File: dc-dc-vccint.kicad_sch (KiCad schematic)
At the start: 61 parts, among them U36 MP8796B, U4 MP8796B

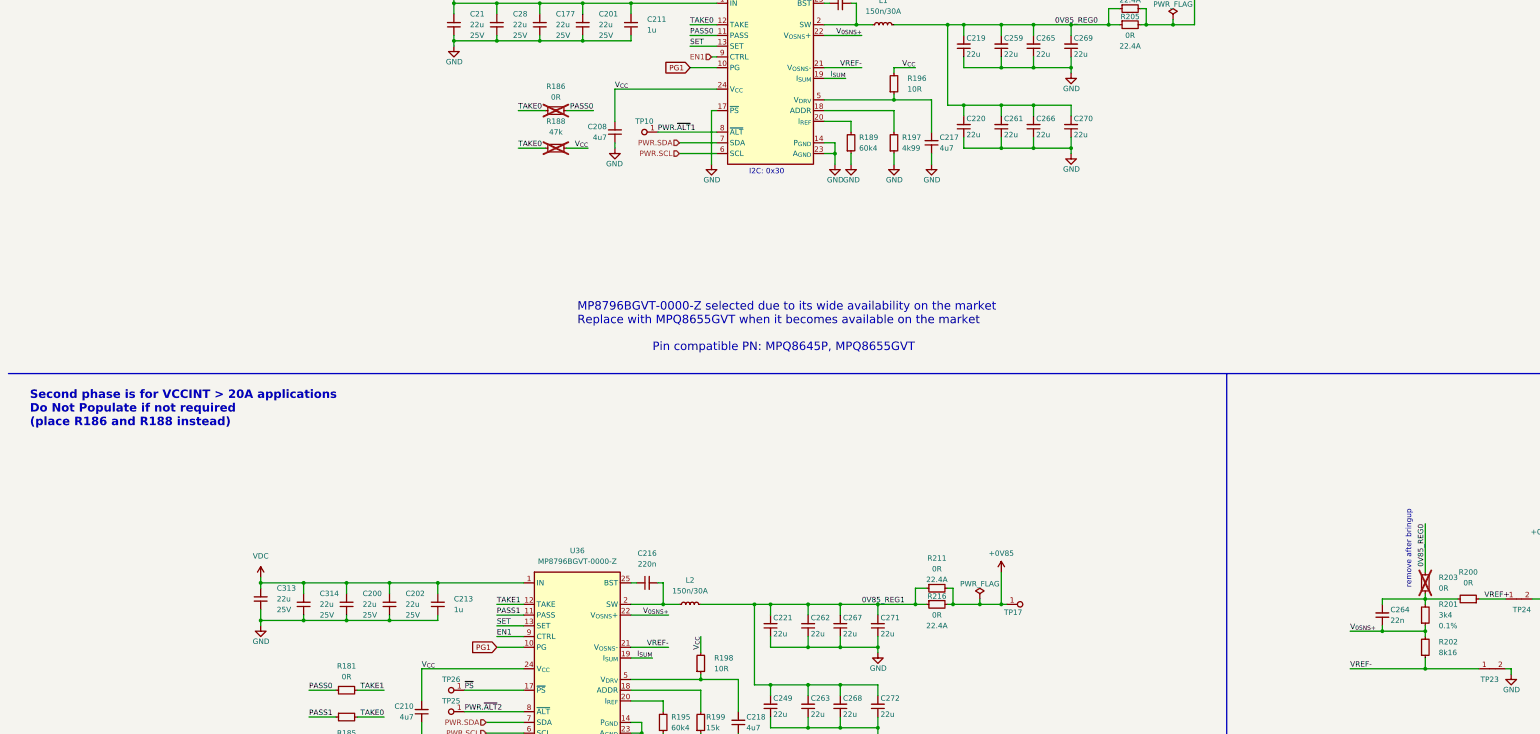
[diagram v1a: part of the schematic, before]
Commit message: [#69428] Set R188 as to be mounted
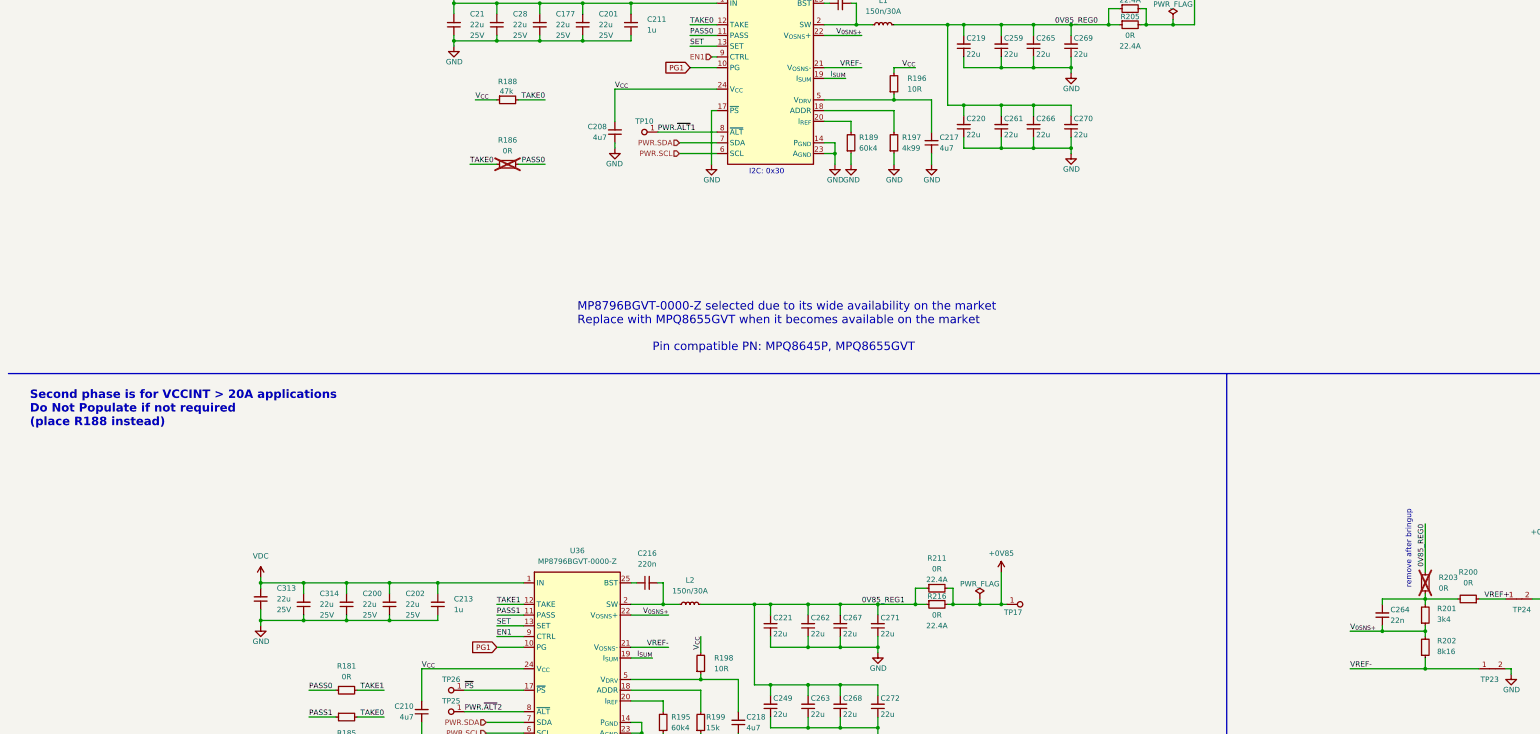
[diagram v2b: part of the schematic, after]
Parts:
- R188: now fitted
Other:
- note added: "Second phase is for VCCINT > 20A applications Do Not Populate if not required (place R188 instead)"
- note removed: "Second phase is for VCCINT > 20A applications Do Not Populate if not required (place R186 and R188 instead)"
- moved on the sheet: R186
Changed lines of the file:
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@@
 	(wire
 		(pts
-			(xy 132.08 87.63) (xy 138.43 87.63)
+			(xy 120.65 100.33) (xy 127 100.33)
 		)
 		(stroke
@@
 	(wire
 		(pts
-			(xy 132.08 96.52) (xy 138.43 96.52)
+			(xy 138.43 85.09) (xy 132.08 85.09)
 		)
 		(stroke
@@
 	(wire
 		(pts
-			(xy 148.59 96.52) (xy 143.51 96.52)
+			(xy 121.92 85.09) (xy 127 85.09)
 		)
 		(stroke
@@
 	(wire
 		(pts
-			(xy 149.86 87.63) (xy 143.51 87.63)
+			(xy 138.43 100.33) (xy 132.08 100.33)
 		)
 		(stroke
@@
 		)
 	)
-	(text "Second phase is for VCCINT > 20A applications\nDo Not Populate if not required \n(place R186 and R188 instead)\n"
+	(text "Second phase is for VCCINT > 20A applications\nDo Not Populate if not required \n(place R188 instead)\n"
 		(exclude_from_sim no)
 		(at 16.51 162.56 0)
@@
 	)
 	(label "PASS0"
-		(at 149.86 87.63 180)
+		(at 138.43 100.33 180)
 		(fields_autoplaced yes)
 		(effects
@@
 	)
 	(label "V_{CC}"
-		(at 148.59 96.52 180)
+		(at 121.92 85.09 0)
 		(fields_autoplaced yes)
 		(effects
@@
 				(size 1.27 1.27)
 			)
-			(justify right bottom)
+			(justify left bottom)
 		)
 	)
@@
 	)
 	(label "TAKE0"
-		(at 132.08 96.52 0)
+		(at 138.43 85.09 180)
 		(fields_autoplaced yes)
 		(effects
@@
 				(size 1.27 1.27)
 			)
-			(justify left bottom)
+			(justify right bottom)
 		)
 	)
@@
 	)
 	(label "TAKE0"
-		(at 132.08 87.63 0)
+		(at 120.65 100.33 0)
 		(fields_autoplaced yes)
 		(effects
@@
 	(symbol
 		(lib_id "antmicroResistors0402:R_0R_0402")
-		(at 138.43 87.63 0)
+		(at 127 100.33 0)
 		(unit 1)
 		(exclude_from_sim no)
@@
 		(fields_autoplaced yes)
 		(property "Reference" "R186"
-			(at 140.97 81.915 0)
+			(at 129.54 94.615 0)
 			(effects
 				(font
@@
 		)
 		(property "Value" "R_0R_0402"
-			(at 158.75 100.33 0)
+			(at 147.32 113.03 0)
 			(effects
 				(font
@@
 		)
 		(property "Footprint" "antmicro-footprints:R_0402_1005Metric"
-			(at 158.75 102.87 0)
+			(at 147.32 115.57 0)
 			(effects
 				(font
@@
 		)
 		(property "Datasheet" "https://industrial.panasonic.com/cdbs/www-data/pdf/RDA0000/AOA0000C301.pdf"
-			(at 158.75 105.41 0)
+			(at 147.32 118.11 0)
 			(effects
 				(font
@@
 		)
 		(property "Description" ""
-			(at 138.43 87.63 0)
+			(at 127 100.33 0)
 			(effects
 				(font
@@
 		)
 		(property "MPN" "ERJ2GE0R00X"
-			(at 158.75 107.95 0)
+			(at 147.32 120.65 0)
 			(effects
 				(font
@@
 		)
 		(property "Manufacturer" "Panasonic"
-			(at 158.75 110.49 0)
+			(at 147.32 123.19 0)
 			(effects
 				(font
@@
 		)
 		(property "License" "Apache-2.0"
-			(at 158.75 113.03 0)
+			(at 147.32 125.73 0)
 			(effects
 				(font
@@
 		)
 		(property "Author" "Antmicro"
-			(at 158.75 115.57 0)
+			(at 147.32 128.27 0)
 			(effects
 				(font
@@
 		)
 		(property "Val" "0R"
-			(at 140.97 84.455 0)
+			(at 129.54 97.155 0)
 			(effects
 				(font
@@
 		)
 		(property "Tolerance" "~"
-			(at 158.75 97.79 0)
+			(at 147.32 110.49 0)
 			(effects
 				(font
@@
 		)
 		(property "Current" "1A"
-			(at 158.75 118.11 0)
+			(at 147.32 130.81 0)
 			(effects
 				(font
@@
 		(on_board yes)
 		(dnp no)
-		(fields_autoplaced yes)
 		(property "Reference" "R201"
-			(at 349.885 204.47 90)
+			(at 349.504 205.486 90)
 			(effects
 				(font
@@
 		)
 		(property "Val" "3k4"
-			(at 349.885 207.01 90)
+			(at 349.504 208.026 90)
 			(effects
 				(font
@@
 				)
 				(justify right)
+				(hide yes)
 			)
 		)
@@
 	(symbol
 		(lib_id "antmicroResistors0402:R_47k_0402")
-		(at 143.51 96.52 180)
+		(at 127 85.09 0)
 		(unit 1)
 		(exclude_from_sim no)
 		(in_bom yes)
 		(on_board yes)
-		(dnp yes)
-		(fields_autoplaced yes)
+		(dnp no)
 		(property "Reference" "R188"
-			(at 140.97 90.17 0)
+			(at 129.54 80.772 0)
 			(effects
 				(font
@@
 		)
 		(property "Value" "R_47k_0402"
-			(at 123.19 83.82 0)
+			(at 147.32 97.79 0)
 			(effects
 				(font
@@
 		)
 		(property "Footprint" "antmicro-footprints:R_0402_1005Metric"
-			(at 123.19 81.28 0)
+			(at 147.32 100.33 0)
 			(effects
 				(font
@@
 		)
 		(property "Datasheet" "https://www.bourns.com/docs/product-datasheets/cr.pdf"
-			(at 123.19 78.74 0)
+			(at 147.32 102.87 0)
 			(effects
 				(font
@@
 		)
 		(property "Description" ""
-			(at 143.51 96.52 0)
+			(at 127 85.09 0)
 			(effects
 				(font
@@
 		)
 		(property "MPN" "CR0402-FX-4702GLF"
-			(at 123.19 76.2 0)
+			(at 147.32 105.41 0)
 			(effects
 				(font
@@
 		)
 		(property "Manufacturer" "Bourns"
-			(at 123.19 73.66 0)
+			(at 147.32 107.95 0)
 			(effects
 				(font
@@
 		)
 		(property "License" "Apache-2.0"
-			(at 123.19 71.12 0)
+			(at 147.32 110.49 0)
 			(effects
 				(font
@@
 		)
 		(property "Author" "Antmicro"
-			(at 123.19 68.58 0)
+			(at 147.32 113.03 0)
 			(effects
 				(font
@@
 		)
 		(property "Val" "47k"
-			(at 140.97 92.71 0)
+			(at 129.286 83.058 0)
 			(effects
 				(font
@@
 		)
 		(property "Tolerance" "1%"
-			(at 123.19 86.36 0)
+			(at 147.32 95.25 0)
 			(effects
 				(font
@@
 		(on_board yes)
 		(dnp no)
-		(fields_autoplaced yes)
 		(property "Reference" "R202"
-			(at 349.885 213.36 90)
+			(at 349.504 213.106 90)
 			(effects
 				(font
@@
 		)
 		(property "Val" "8k16"
-			(at 349.885 215.9 90)
+			(at 349.504 215.646 90)
 			(effects
 				(font

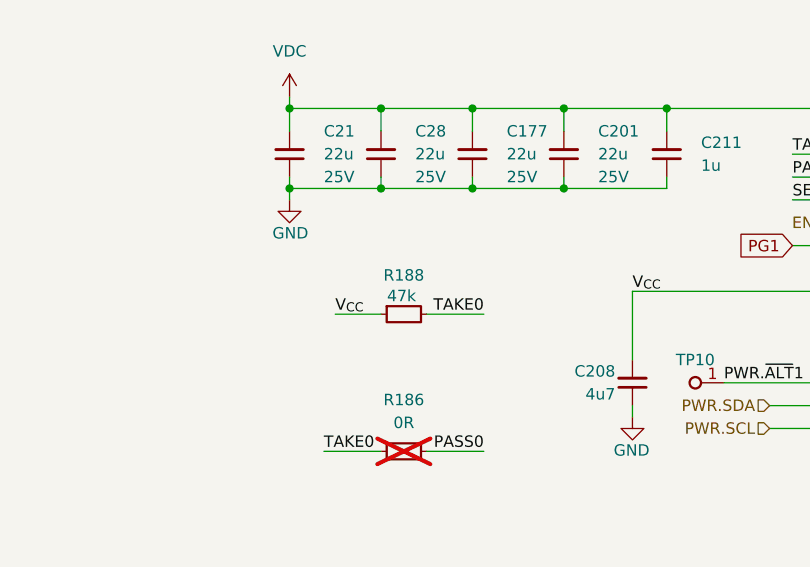
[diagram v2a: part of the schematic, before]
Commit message: [#69518] Fix Q20 configuration
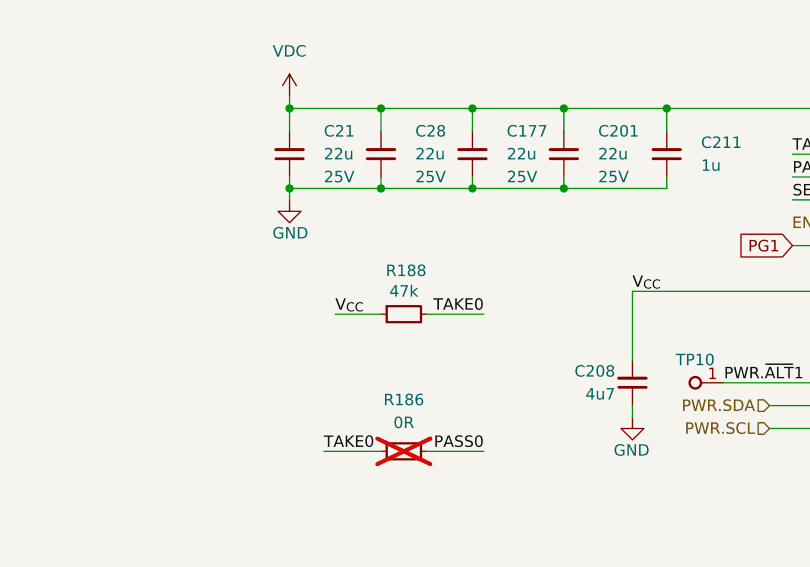
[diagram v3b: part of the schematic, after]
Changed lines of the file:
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@@
 		(dnp no)
 		(property "Reference" "R188"
-			(at 129.54 80.772 0)
+			(at 129.794 80.264 0)
 			(effects
 				(font
@@
 		)
 		(property "Val" "47k"
-			(at 129.286 83.058 0)
+			(at 129.54 82.55 0)
 			(effects
 				(font

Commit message: [#69629] Fix DNP attributes
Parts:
- R186: now left out of the parts list

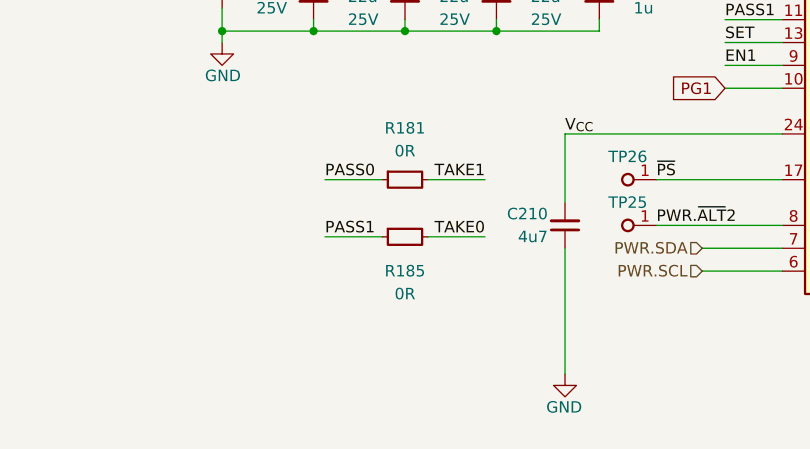
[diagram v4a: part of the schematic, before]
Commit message: [#69602] Add U36 phase shedding pullup
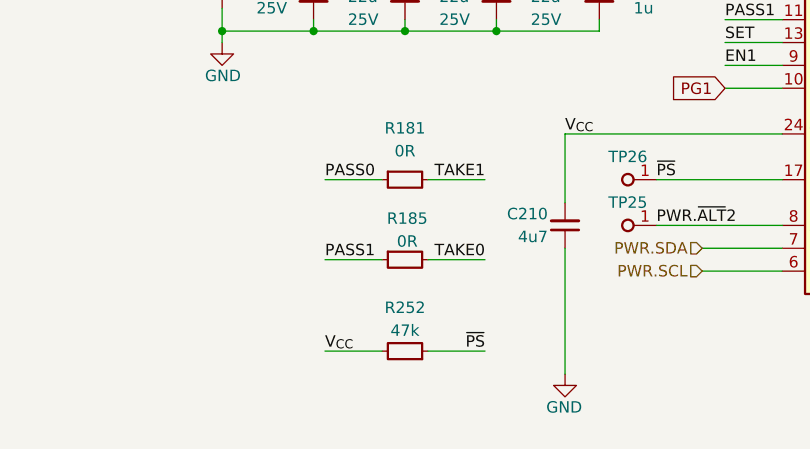
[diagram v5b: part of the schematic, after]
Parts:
- added R252: R_47k_0402, antmicro-footprints:R_0402_1005Metric, symbol antmicroResistors0402:R_47k_0402
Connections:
- net V_{CC}: now also R252.2
- net ~{PS}: now also R252.1
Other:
- moved on the sheet: R185

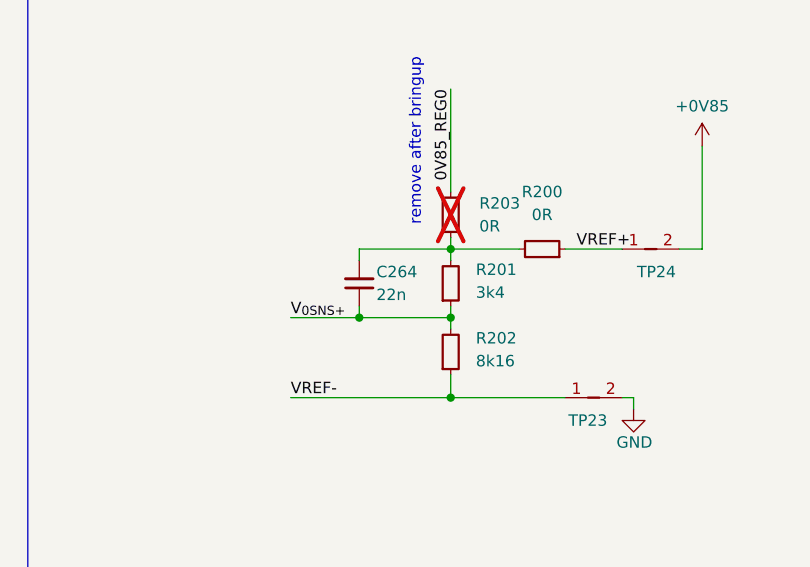
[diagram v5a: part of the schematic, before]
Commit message: [#69547] Replace VCCINT feed-forward capacitor to 22p
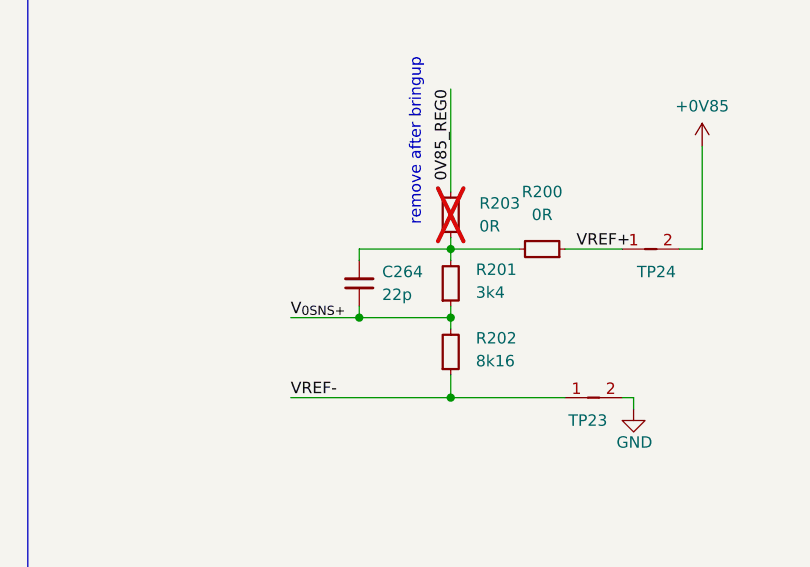
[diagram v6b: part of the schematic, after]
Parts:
- removed C264: C_22n_0402, antmicro-footprints:C_0402_1005Metric, symbol antmicroCapacitors0402:C_22n_0402
- added C264: C_22p_0402, antmicro-footprints:C_0402_1005Metric, symbol antmicroCapacitors0402:C_22p_0402
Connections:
- net V_{0SNS+}: now also C264.1
- net at R200.2, R201.2, R203.1: now also C264.2
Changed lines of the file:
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@@
 	)
 	(symbol
-		(lib_id "antmicroCapacitors0402:C_22n_0402")
-		(at 336.55 209.55 90)
-		(unit 1)
-		(exclude_from_sim no)
-		(in_bom yes)
-		(on_board yes)
-		(dnp no)
-		(property "Reference" "C264"
-			(at 338.455 205.74 90)
-			(effects
-				(font
-					(size 1.27 1.27)
-					(thickness 0.15)
-				)
-				(justify right)
-			)
-		)
-		(property "Value" "C_22n_0402"
-			(at 346.71 189.23 0)
-			(effects
-				(font
-					(size 1.27 1.27)
-					(thickness 0.15)
-				)
-				(justify left bottom)
-				(hide yes)
-			)
-		)
-		(property "Footprint" "antmicro-footprints:C_0402_1005Metric"
-			(at 349.25 189.23 0)
-			(effects
-				(font
-					(size 1.27 1.27)
-					(thickness 0.15)
-				)
-				(justify left bottom)
-				(hide yes)
-			)
-		)
-		(property "Datasheet" "https://www.murata.com/products/productdetail?partno=GCM155R71H223MA55%23"
-			(at 351.79 189.23 0)
-			(effects
-				(font
-					(size 1.27 1.27)
-					(thickness 0.15)
-				)
-				(justify left bottom)
-				(hide yes)
-			)
-		)
-		(property "Description" ""
-			(at 336.55 209.55 0)
-			(effects
-				(font
-					(size 1.27 1.27)
-				)
-				(hide yes)
-			)
-		)
-		(property "MPN" "GCM155R71H223MA55D"
-			(at 354.33 189.23 0)
-			(effects
-				(font
-					(size 1.27 1.27)
-					(thickness 0.15)
-				)
-				(justify left bottom)
-				(hide yes)
-			)
-		)
-		(property "Manufacturer" "Murata"
-			(at 356.87 189.23 0)
-			(effects
-				(font
-					(size 1.27 1.27)
-					(thickness 0.15)
-				)
-				(justify left bottom)
-				(hide yes)
-			)
-		)
-		(property "License" "Apache-2.0"
-			(at 359.41 189.23 0)
-			(effects
-				(font
-					(size 1.27 1.27)
-					(thickness 0.15)
-				)
-				(justify left bottom)
-				(hide yes)
-			)
-		)
-		(property "Author" "Antmicro"
-			(at 361.95 189.23 0)
-			(effects
-				(font
-					(size 1.27 1.27)
-					(thickness 0.15)
-				)
-				(justify left bottom)
-				(hide yes)
-			)
-		)
-		(property "Val" "22n"
-			(at 338.455 208.28 90)
-			(effects
-				(font
-					(size 1.27 1.27)
-					(thickness 0.15)
-				)
-				(justify right)
-			)
-		)
-		(property "Voltage" ""
-			(at 364.49 189.23 0)
-			(effects
-				(font
-					(size 1.27 1.27)
-				)
-				(justify left bottom)
-				(hide yes)
-			)
-		)
-		(property "Dielectric" ""
-			(at 367.03 189.23 0)
-			(effects
-				(font
-					(size 1.27 1.27)
-				)
-				(justify left bottom)
-				(hide yes)
-			)
-		)
-		(pin "1"
-		)
-		(pin "2"
-		)
-		(instances
-			(project "data-center-rdimm-ddr5-tester"
-				(path "/1faa6543-e26a-4449-8bac-ee14b9f19e5f/00000000-0000-0000-0000-000060225b0c/3cfc3a6a-24b0-4207-8c35-05eeccc29696"
-					(reference "C264")
-					(unit 1)
-				)
-			)
-		)
-	)
-	(symbol
 		(lib_id "antmicropower:GND")
 		(at 207.01 100.33 0)
@@
 					(unit 1)
 				)
+			)
+		)
+	)
+	(symbol
+		(lib_id "antmicroCapacitors0402:C_22p_0402")
+		(at 336.55 209.55 90)
+		(unit 1)
+		(exclude_from_sim no)
+		(in_bom yes)
+		(on_board yes)
+		(dnp no)
+		(fields_autoplaced yes)
+		(property "Reference" "C264"
+			(at 339.09 205.7336 90)
+			(effects
+				(font
+					(size 1.27 1.27)
+					(thickness 0.15)
+				)
+				(justify right)
+			)
+		)
+		(property "Value" "C_22p_0402"
+			(at 346.71 189.23 0)
+			(effects
+				(font
+					(size 1.27 1.27)
+					(thickness 0.15)
+				)
+				(justify left bottom)
+				(hide yes)
+			)
+		)
+		(property "Footprint" "antmicro-footprints:C_0402_1005Metric"
+			(at 349.25 189.23 0)
+			(effects
+				(font
+					(size 1.27 1.27)
+					(thickness 0.15)
+				)
+				(justify left bottom)
+				(hide yes)
+			)
+		)
+		(property "Datasheet" "https://www.yageo.com/en/Chart/Download/pdf/CC0402JRNPO9BN220"
+			(at 351.79 189.23 0)
+			(effects
+				(font
+					(size 1.27 1.27)
+					(thickness 0.15)
+				)
+				(justify left bottom)
+				(hide yes)
+			)
+		)
+		(property "Description" "SMD Multilayer Ceramic Capacitor, 22 pF, 50 V, 0402 [1005 Metric], ± 5%, C0G / NP0, CC Series"
+			(at 336.55 209.55 0)
+			(effects
+				(font
+					(size 1.27 1.27)
+				)
+				(hide yes)
+			)
+		)
+		(property "MPN" "CC0402JRNPO9BN220"
+			(at 354.33 189.23 0)
+			(effects
+				(font
+					(size 1.27 1.27)
+					(thickness 0.15)
+				)
+				(justify left bottom)
+				(hide yes)
+			)
+		)
+		(property "Manufacturer" "YAGEO"
+			(at 356.87 189.23 0)
+			(effects
+				(font
+					(size 1.27 1.27)
+					(thickness 0.15)
+				)
+				(justify left bottom)
+				(hide yes)
+			)
+		)
+		(property "License" "Apache-2.0"
+			(at 359.41 189.23 0)
+			(effects
+				(font
+					(size 1.27 1.27)
+					(thickness 0.15)
+				)
+				(justify left bottom)
+				(hide yes)
+			)
+		)
+		(property "Author" "Antmicro"
+			(at 361.95 189.23 0)
+			(effects
+				(font
+					(size 1.27 1.27)
+					(thickness 0.15)
+				)
+				(justify left bottom)
+				(hide yes)
+			)
+		)
+		(property "Val" "22p"
+			(at 339.09 208.2736 90)
+			(effects
+				(font
+					(size 1.27 1.27)
+					(thickness 0.15)
+				)
+				(justify right)
+			)
+		)
+		(property "Voltage" ""
+			(at 364.49 189.23 0)
+			(effects
+				(font
+					(size 1.27 1.27)
+				)
+				(justify left bottom)
+				(hide yes)
+			)
+		)
+		(property "Dielectric" ""
+			(at 367.03 189.23 0)
+			(effects
+				(font
+					(size 1.27 1.27)
+				)
+				(justify left bottom)
+				(hide yes)
+			)
+		)
+		(pin "2"
+		)
+		(pin "1"
+		)
+		(instances
+			(project ""
+				(path "/1faa6543-e26a-4449-8bac-ee14b9f19e5f/00000000-0000-0000-0000-000060225b0c/3cfc3a6a-24b0-4207-8c35-05eeccc29696"
+					(reference "C264")
+					(unit 1)
+				)
